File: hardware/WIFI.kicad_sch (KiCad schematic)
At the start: 37 parts

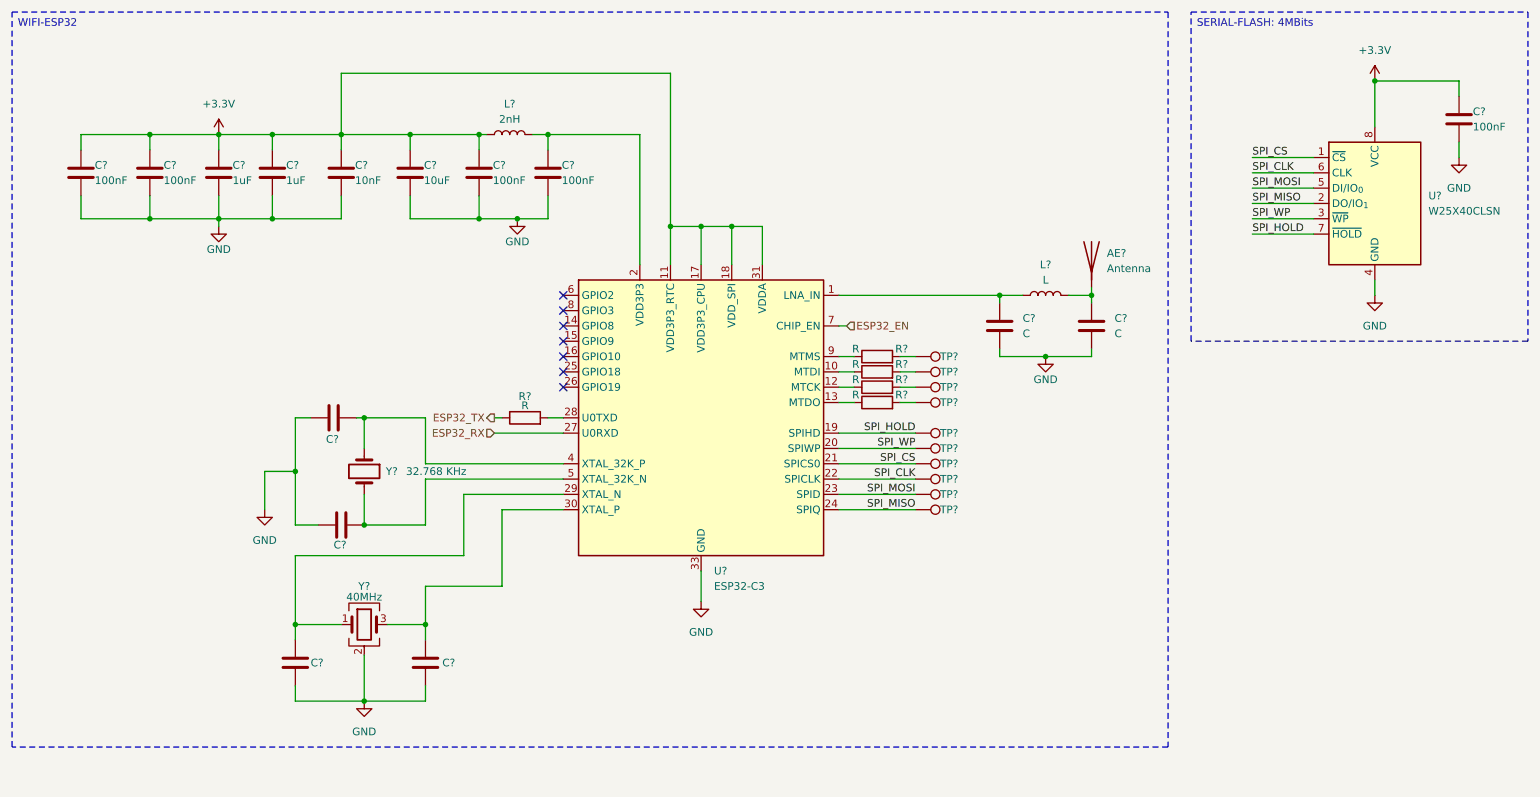
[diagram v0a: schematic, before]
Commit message: Change ESP32 module to stand-alone, change regulator for wide input range, modify location of certain things on MCU_Unit.
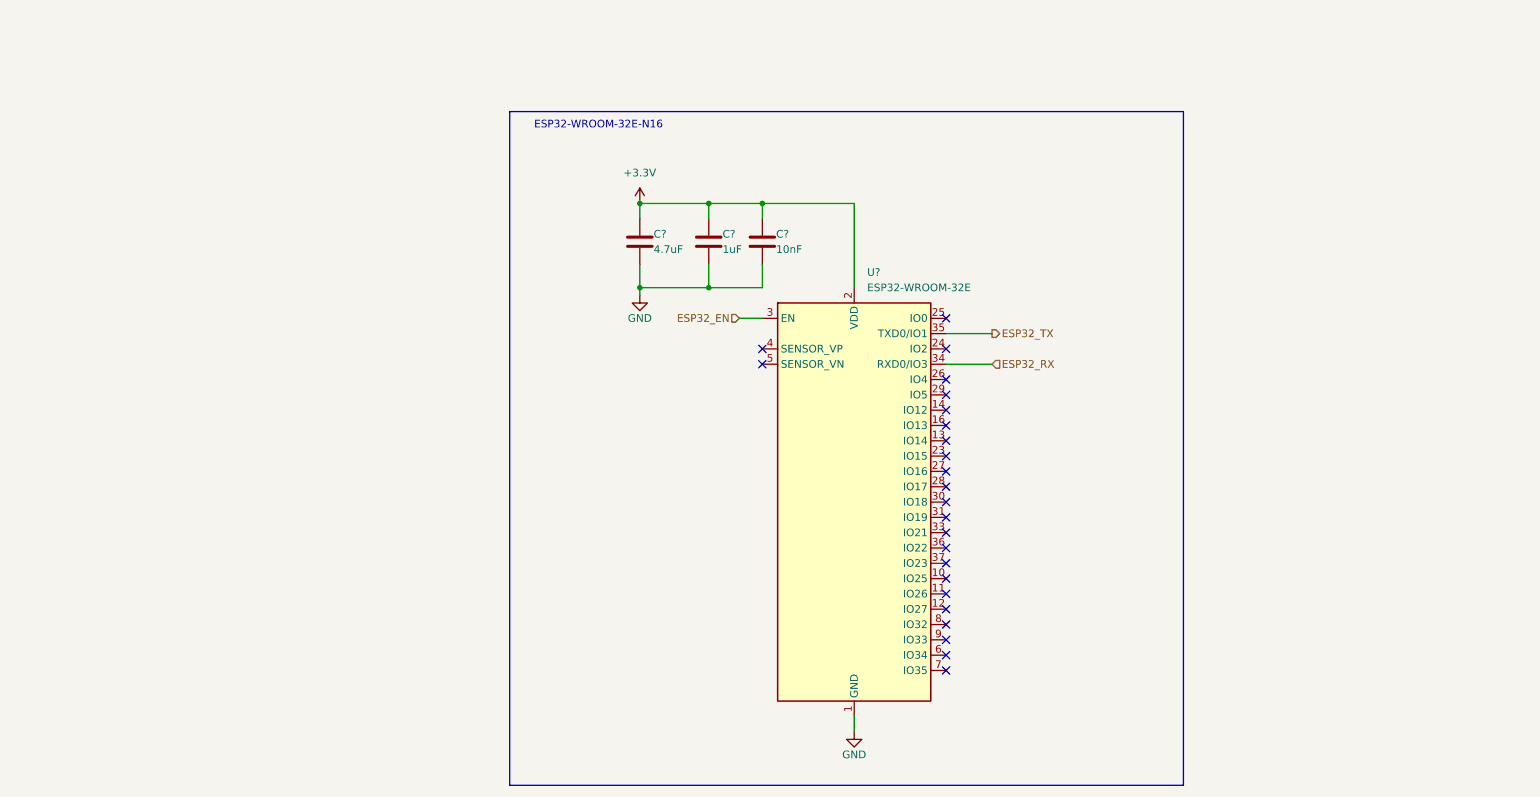
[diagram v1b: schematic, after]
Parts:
- removed AE?: Antenna, Connector_Coaxial:U.FL_Molex_MCRF_73412-0110_Vertical, symbol Device:Antenna
- removed C?: 10uF, Capacitor_SMD:C_0805_2012Metric_Pad1.18x1.45mm_HandSolder, symbol Device:C
- removed C? (x2): C, symbol Device:C
- removed C? (x5): 100nF, Capacitor_SMD:C_0805_2012Metric_Pad1.18x1.45mm_HandSolder, symbol Device:C
- removed C? (x4): ~, Capacitor_SMD:C_0805_2012Metric_Pad1.18x1.45mm_HandSolder, symbol Device:C
- removed L?: 2nH, symbol Device:L
- removed L?: L, symbol Device:L
- removed R? (x5): R, symbol Device:R
- removed TP? (x10): TestPoint, symbol Connector:TestPoint
- removed U?: W25X40CLSN, Package_SO:SOIC-8_3.9x4.9mm_P1.27mm, symbol Memory_Flash:W25X40CLSN
- removed U?: ESP32-C3, Package_DFN_QFN:QFN-32-1EP_5x5mm_P0.5mm_EP3.7x3.7mm, symbol MCU_Espressif:ESP32-C3
- removed Y?: 32.768 KHz, symbol Device:Crystal
- removed Y?: 40MHz, symbol Device:Crystal_GND24
- added U?: ESP32-WROOM-32E, RF_Module:ESP32-WROOM-32D, symbol RF_Module:ESP32-WROOM-32E
- C?: value 1uF -> 4.7uF
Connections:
- net +3.3V: now also U?.2 (VDD)
- net ESP32_EN: now also U?.3 (EN)
- net ESP32_RX: now also U?.34 (RXD0/IO3)
- net ESP32_TX: now also U?.35 (TXD0/IO1)
- net GND: now also U?.1 (GND), U?.15 (GND), U?.38 (GND), U?.39 (GND)
- no-connect marks 7 -> 24
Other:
- note added: "ESP32-WROOM-32E-N16"
- moved on the sheet: C?

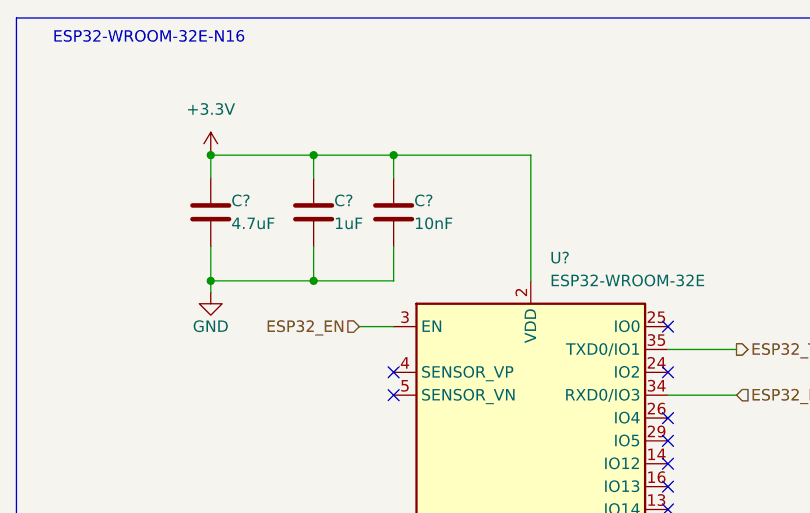
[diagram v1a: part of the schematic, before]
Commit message: Assign footprints to some components and improvements.
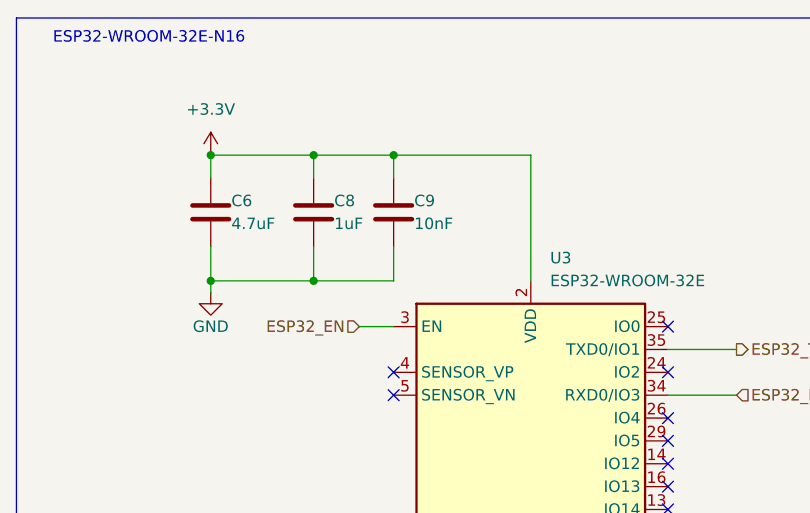
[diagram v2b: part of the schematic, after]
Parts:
- C6, C8, C9: renamed from C?; footprint Capacitor_SMD:C_0805_2012Metric_Pad1.18x1.45mm_HandSolder -> Capacitor_SMD:C_0603_1608Metric_Pad1.08x0.95mm_HandSolder
- gave numbers to parts that had none: 1
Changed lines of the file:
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@@
 		(on_board yes)
 		(dnp no)
-		(property "Reference" "C?"
+		(property "Reference" "C8"
 			(at 140.716 57.15 0)
 			(effects
@@
 			)
 		)
-		(property "Footprint" "Capacitor_SMD:C_0805_2012Metric_Pad1.18x1.45mm_HandSolder"
+		(property "Footprint" "Capacitor_SMD:C_0603_1608Metric_Pad1.08x0.95mm_HandSolder"
 			(at 139.3952 62.23 0)
 			(effects
@@
 		(dnp no)
 		(fields_autoplaced yes)
-		(property "Reference" "#PWR?"
+		(property "Reference" "#PWR02"
 			(at 127 55.88 0)
 			(effects
@@
 		(on_board yes)
 		(dnp no)
-		(property "Reference" "C?"
+		(property "Reference" "C6"
 			(at 129.286 57.15 0)
 			(effects
@@
 			)
 		)
-		(property "Footprint" "Capacitor_SMD:C_0805_2012Metric_Pad1.18x1.45mm_HandSolder"
+		(property "Footprint" "Capacitor_SMD:C_0603_1608Metric_Pad1.08x0.95mm_HandSolder"
 			(at 127.9652 62.23 0)
 			(effects
@@
 		(dnp no)
 		(fields_autoplaced yes)
-		(property "Reference" "U?"
+		(property "Reference" "U3"
 			(at 164.7033 63.5 0)
 			(effects
@@
 		(on_board yes)
 		(dnp no)
-		(property "Reference" "#PWR?"
+		(property "Reference" "#PWR04"
 			(at 127 73.66 0)
 			(effects
@@
 		(on_board yes)
 		(dnp no)
-		(property "Reference" "#PWR?"
+		(property "Reference" "#PWR01"
 			(at 162.56 146.05 0)
 			(effects
@@
 		(on_board yes)
 		(dnp no)
-		(property "Reference" "C?"
+		(property "Reference" "C9"
 			(at 149.606 57.15 0)
 			(effects
@@
 			)
 		)
-		(property "Footprint" "Capacitor_SMD:C_0805_2012Metric_Pad1.18x1.45mm_HandSolder"
+		(property "Footprint" "Capacitor_SMD:C_0603_1608Metric_Pad1.08x0.95mm_HandSolder"
 			(at 148.2852 62.23 0)
 			(effects

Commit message: Improvements to schematic.
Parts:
- renumbered C8 to C?, C6 to C?, C9 to C?, U3 to U?
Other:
- company: (none) -> FEYTECH PTY LTD
- title: (none) -> MQTT Gateway
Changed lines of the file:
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@@
 	(generator_version "9.0")
 	(paper "A4")
+	(title_block
+		(title "MQTT Gateway")
+		(date "2026-03-13")
+		(rev "V1.0.0")
+		(company "FEYTECH PTY LTD")
+	)
 	(rectangle
 		(start 105.41 36.83)
@@
 		(on_board yes)
 		(dnp no)
-		(property "Reference" "C8"
+		(property "Reference" "C?"
 			(at 140.716 57.15 0)
 			(effects
@@
 			(project "WIFI"
 				(path "/0fc824bd-7cd8-4f9b-8387-ef1499f470b4"
-					(reference "C8")
+					(reference "C?")
 					(unit 1)
 				)
@@
 		(dnp no)
 		(fields_autoplaced yes)
-		(property "Reference" "#PWR02"
+		(property "Reference" "#PWR?"
 			(at 127 55.88 0)
 			(effects
@@
 			(project "WIFI"
 				(path "/0fc824bd-7cd8-4f9b-8387-ef1499f470b4"
-					(reference "#PWR02")
+					(reference "#PWR?")
 					(unit 1)
 				)
@@
 		(on_board yes)
 		(dnp no)
-		(property "Reference" "C6"
+		(property "Reference" "C?"
 			(at 129.286 57.15 0)
 			(effects
@@
 			(project "WIFI"
 				(path "/0fc824bd-7cd8-4f9b-8387-ef1499f470b4"
-					(reference "C6")
+					(reference "C?")
 					(unit 1)
 				)
@@
 		(dnp no)
 		(fields_autoplaced yes)
-		(property "Reference" "U3"
+		(property "Reference" "U?"
 			(at 164.7033 63.5 0)
 			(effects
@@
 			(project ""
 				(path "/0fc824bd-7cd8-4f9b-8387-ef1499f470b4"
-					(reference "U3")
+					(reference "U?")
 					(unit 1)
 				)
@@
 		(on_board yes)
 		(dnp no)
-		(property "Reference" "#PWR04"
+		(property "Reference" "#PWR?"
 			(at 127 73.66 0)
 			(effects
@@
 			(project "WIFI"
 				(path "/0fc824bd-7cd8-4f9b-8387-ef1499f470b4"
-					(reference "#PWR04")
+					(reference "#PWR?")
 					(unit 1)
 				)
@@
 		(on_board yes)
 		(dnp no)
-		(property "Reference" "#PWR01"
+		(property "Reference" "#PWR?"
 			(at 162.56 146.05 0)
 			(effects
@@
 			(project "WIFI"
 				(path "/0fc824bd-7cd8-4f9b-8387-ef1499f470b4"
-					(reference "#PWR01")
+					(reference "#PWR?")
 					(unit 1)
 				)
@@
 		(on_board yes)
 		(dnp no)
-		(property "Reference" "C9"
+		(property "Reference" "C?"
 			(at 149.606 57.15 0)
 			(effects
@@
 			(project "WIFI"
 				(path "/0fc824bd-7cd8-4f9b-8387-ef1499f470b4"
-					(reference "C9")
-					(unit 1)
-				)
+					(reference "C?")
+					(unit 1)
+				)

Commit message: Improvements
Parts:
- gave numbers to parts that had none: 4
